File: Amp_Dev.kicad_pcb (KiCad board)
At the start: 2 copper layers, 100 x 100 mm, 760 parts, among them J1 SMA, J10 SMA, J11 CONN_01X02, J12 TEST_1P, J13 SMA, J14 CONN_01X02, J16 TEST_1P, J17 TEST_1P, J18 TEST_1P, J2 SMA, J20 SMA, J21 SMA, J22 SMA, J3 TEST_1P, J4 TEST_1P, J5 CONN_01X03, J6 TEST_1P, J7 CONN_01X03, J8 TEST_1P, J9 TEST_1P, Q1 DMN2075U, U1 MML09211H, U2 RF6886, U3 LMV358, U4 SN74LVC1G17, U5 TLV702, U6 LTC2644, U7 RT9183

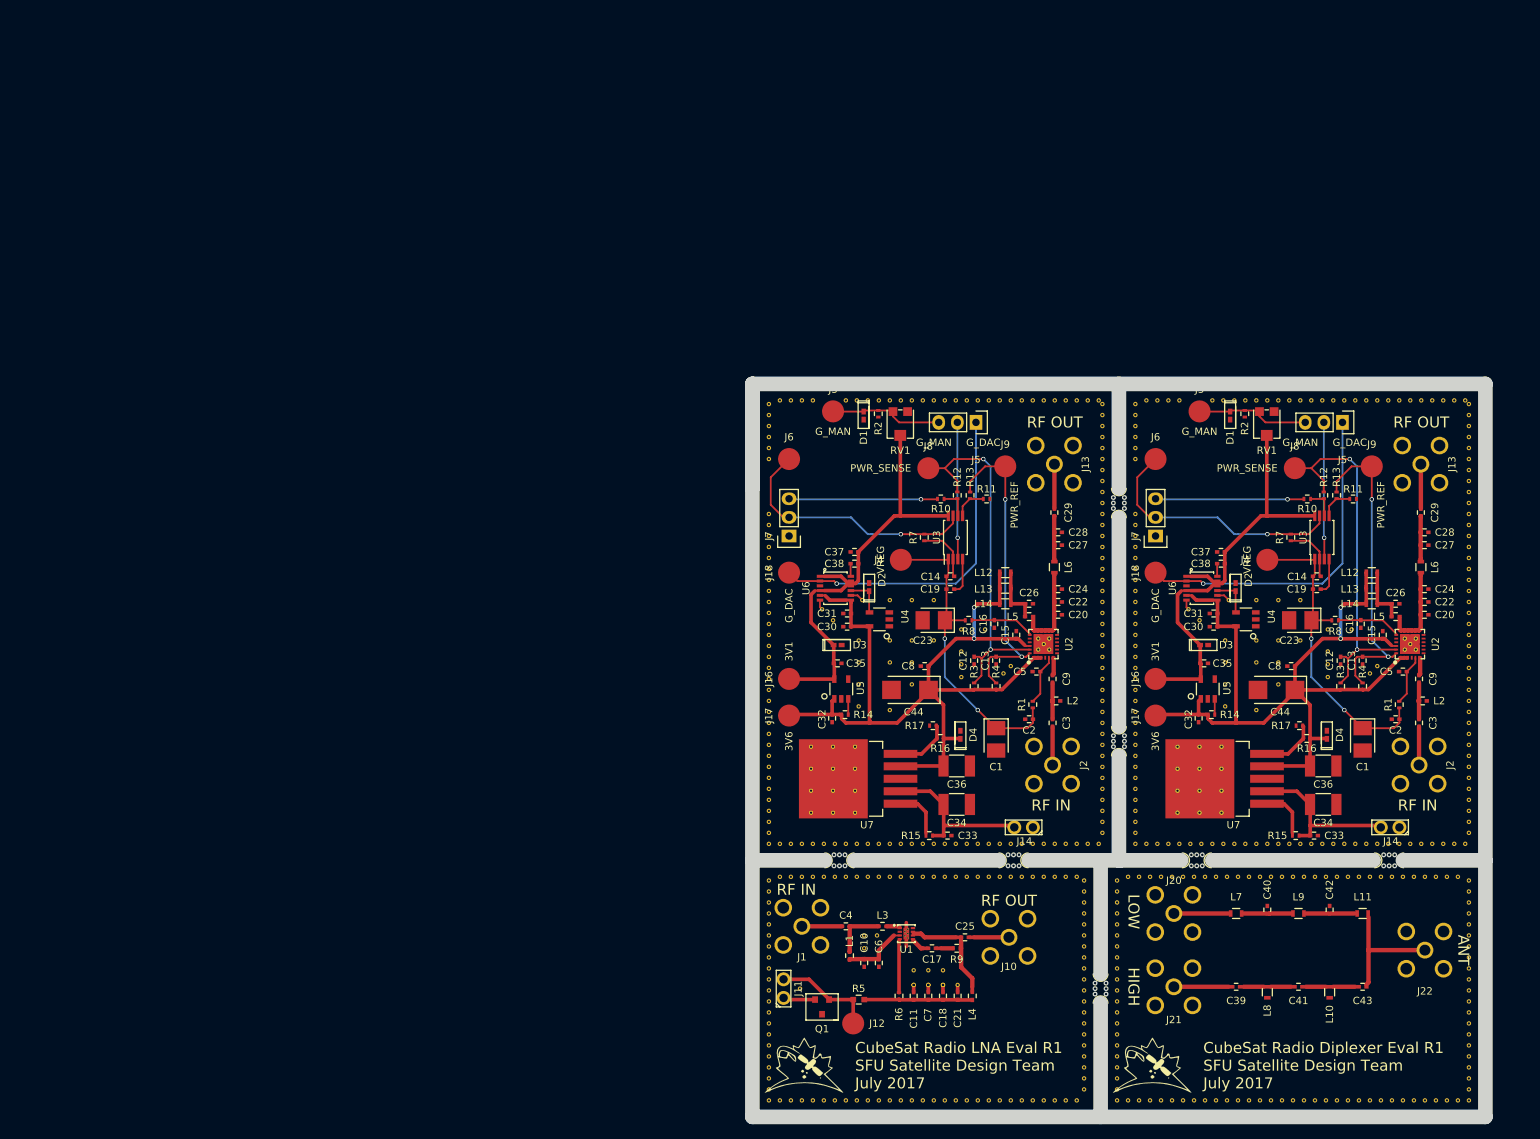
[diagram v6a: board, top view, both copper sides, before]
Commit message: added PA control header. resolves #7
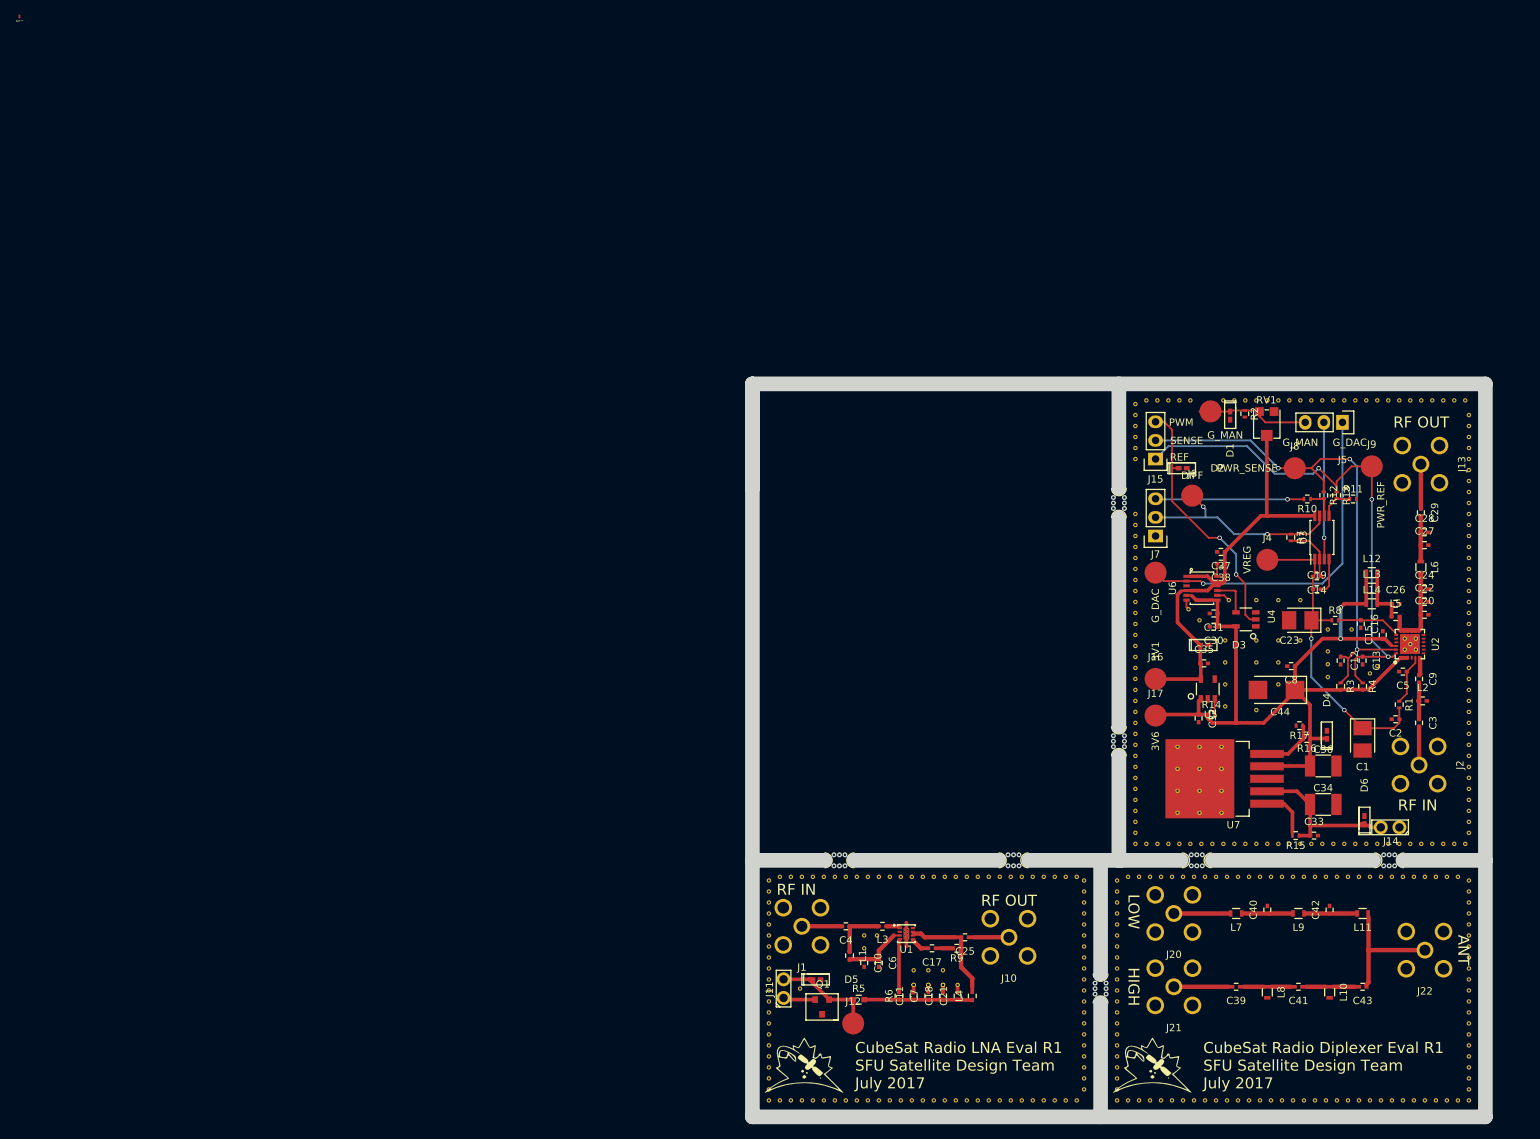
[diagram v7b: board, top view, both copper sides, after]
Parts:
- removed the C1 at (133.2, 98.5)
- removed the C12 at (130.2, 87.8)
- removed the C13 at (133.2, 87.8)
- removed the C14 at (127.0, 76.2)
- removed the C15 at (136.0, 84.2)
- removed the C16 at (133.0, 82.8)
- removed the C19 at (127.0, 78.0)
- removed the C2 at (137.8, 95.8)
- removed the C20 at (141.7, 81.5)
- removed the C22 at (141.7, 79.8)
- removed the C23 at (124.8, 82.2)
- removed the C24 at (141.7, 78.0)
- removed the C26 at (137.8, 80.0)
- removed the C27 at (141.7, 72.0)
- removed the C28 at (141.7, 70.2)
- removed the C29 at (141.2, 67.5)
- removed the C3 at (140.9, 96.2)
- removed the C30 at (112.9, 83.1)
- removed the C31 at (112.9, 81.3)
- removed the C32 at (110.9, 95.6)
- removed the C33 at (126.6, 111.6)
- removed the C34 at (127.9, 107.4)
- removed the C35 at (111.6, 88.1)
- removed the C36 at (127.9, 102.1)
- removed the C37 at (113.9, 72.9)
- removed the C38 at (113.9, 74.5)
- removed the C44 at (121.5, 91.8)
- removed the C5 at (138.8, 89.2)
- removed the C8 at (123.5, 88.5)
- removed the C9 at (140.9, 90.2)
- removed the D1 at (115.2, 54.3)
- removed the D2 at (115.9, 77.7)
- removed the D3 at (111.6, 85.6)
- removed the D4 at (128.4, 97.9)
- removed the G*** at (107.8, 105.8)
- removed the J13 at (141.2, 61.0)
- removed the J14 at (137.0, 110.5)
- removed the J16 at (105.0, 90.2)
- removed the J17 at (105.0, 95.2)
- removed the J18 at (105.0, 75.8)
- removed the J2 at (140.9, 102.0)
- removed the J3 at (111.0, 53.8)
- removed the J4 at (120.2, 74.0)
- removed the J5 at (130.5, 55.2)
- removed the J6 at (105.0, 60.2)
- removed the J7 at (105.0, 70.8)
- removed the J8 at (124.0, 61.5)
- removed the J9 at (134.5, 61.2)
- removed the L12 at (134.5, 75.8)
- removed the L13 at (134.5, 77.9)
- removed the L14 at (134.5, 80.0)
- removed the L2 at (141.4, 93.2)
- removed the L5 at (137.8, 81.8)
- removed the L6 at (141.2, 75.0)
- removed the R1 at (138.2, 93.8)
- removed the R10 at (125.7, 65.7)
- removed the R11 at (131.9, 65.7)
- removed the R12 at (128.0, 65.2)
- removed the R13 at (129.7, 65.2)
- removed the R14 at (112.6, 95.1)
- removed the R15 at (124.1, 111.6)
- removed the R16 at (125.6, 98.4)
- removed the R17 at (124.6, 96.6)
- removed the R2 at (117.2, 54.1)
- removed the R3 at (130.2, 91.2)
- removed the R4 at (133.2, 91.2)
- removed the R7 at (123.5, 71.0)
- removed the R8 at (129.5, 82.2)
- removed the REF** at (139.0, 84.8)
- removed the REF** at (102.2, 109.8)
- removed the REF** at (147.8, 73.8)
- removed the REF** at (147.8, 72.2)
- removed the REF** at (147.8, 70.8)
- removed the REF** at (147.8, 69.2)
- removed the REF** at (147.8, 67.8)
- removed the REF** at (147.8, 66.2)
- removed the REF** at (147.8, 64.8)
- removed the REF** at (147.8, 63.2)
- removed the REF** at (147.8, 61.8)
- removed the REF** at (147.8, 60.2)
- removed the REF** at (102.2, 108.2)
- removed the REF** at (147.8, 58.8)
- removed the REF** at (147.8, 57.2)
- removed the REF** at (147.8, 55.8)
- removed the REF** at (147.8, 54.2)
- removed the REF** at (147.8, 52.8)
- removed the REF** at (103.8, 52.2)
- removed the REF** at (105.2, 52.2)
- removed the REF** at (106.8, 52.2)
- removed the REF** at (108.2, 52.2)
- removed the REF** at (112.8, 52.2)
- removed the REF** at (102.2, 106.8)
- removed the REF** at (114.2, 52.2)
- removed the REF** at (115.8, 52.2)
- removed the REF** at (117.2, 52.2)
- removed the REF** at (118.8, 52.2)
- removed the REF** at (120.2, 52.2)
- removed the REF** at (121.8, 52.2)
- removed the REF** at (123.2, 52.2)
- removed the REF** at (124.8, 52.2)
- removed the REF** at (126.2, 52.2)
- removed the REF** at (127.8, 52.2)
- removed the REF** at (102.2, 105.2)
- removed the REF** at (129.2, 52.2)
- removed the REF** at (130.8, 52.2)
- removed the REF** at (132.2, 52.2)
- removed the REF** at (133.8, 52.2)
- removed the REF** at (135.2, 52.2)
- removed the REF** at (136.8, 52.2)
- removed the REF** at (138.2, 52.2)
- removed the REF** at (139.8, 52.2)
- removed the REF** at (141.2, 52.2)
- removed the REF** at (142.8, 52.2)
- removed the REF** at (102.2, 103.8)
- removed the REF** at (144.2, 52.2)
- removed the REF** at (145.8, 52.2)
- removed the REF** at (147.2, 52.2)
- removed the REF** at (128.5, 90.0)
- removed the REF** at (128.5, 88.2)
- removed the REF** at (128.5, 86.5)
- removed the REF** at (134.2, 89.5)
- removed the REF** at (128.5, 83.5)
- removed the REF** at (131.8, 83.5)
- removed the REF** at (108.0, 99.5)
- removed the REF** at (102.2, 102.2)
- removed the REF** at (111.0, 99.5)
- removed the REF** at (114.0, 99.5)
- removed the REF** at (108.0, 102.5)
- removed the REF** at (111.0, 102.5)
- removed the REF** at (114.0, 102.5)
- removed the REF** at (108.0, 105.5)
- removed the REF** at (111.0, 105.5)
- removed the REF** at (114.0, 105.5)
- removed the REF** at (108.0, 108.5)
- removed the REF** at (111.0, 108.5)
- removed the REF** at (102.2, 100.8)
- removed the REF** at (114.0, 108.5)
- removed the REF** at (109.5, 80.8)
- removed the REF** at (118.8, 79.5)
- removed the REF** at (121.8, 79.5)
- removed the REF** at (124.8, 79.5)
- removed the REF** at (118.8, 85.0)
- removed the REF** at (124.8, 85.0)
- removed the REF** at (121.8, 85.0)
- removed the REF** at (118.8, 88.0)
- removed the REF** at (121.8, 88.0)
- removed the REF** at (102.2, 99.2)
- removed the REF** at (118.8, 94.5)
- removed the REF** at (121.8, 91.0)
- removed the REF** at (111.0, 82.2)
- removed the REF** at (114.5, 85.0)
- removed the REF** at (114.5, 88.0)
- removed the REF** at (114.5, 91.0)
- removed the REF** at (114.5, 94.0)
- removed the REF** at (102.2, 97.8)
- removed the REF** at (102.2, 96.2)
- removed the REF** at (139.0, 86.2)
- removed the REF** at (102.2, 94.8)
- removed the REF** at (102.2, 93.2)
- removed the REF** at (102.2, 91.8)
- removed the REF** at (102.2, 90.2)
- removed the REF** at (102.2, 88.8)
- removed the REF** at (102.2, 87.2)
- removed the REF** at (102.2, 85.8)
- removed the REF** at (102.2, 84.2)
- removed the REF** at (102.2, 82.8)
- removed the REF** at (102.2, 81.2)
- removed the REF** at (140.5, 86.2)
- removed the REF** at (102.2, 79.8)
- removed the REF** at (102.2, 78.2)
- removed the REF** at (102.2, 76.8)
- removed the REF** at (102.2, 75.2)
- removed the REF** at (102.2, 73.8)
- removed the REF** at (102.2, 72.2)
- removed the REF** at (102.2, 70.8)
- removed the REF** at (102.2, 69.2)
- removed the REF** at (102.2, 67.8)
- removed the REF** at (102.2, 60.2)
- removed the REF** at (140.5, 84.8)
- removed the REF** at (102.2, 58.8)
- removed the REF** at (102.2, 57.2)
- removed the REF** at (102.2, 55.8)
- removed the REF** at (102.2, 54.2)
- removed the REF** at (102.2, 52.8)
- removed the REF** at (197.8, 52.8)
- removed the REF** at (103.8, 112.8)
- removed the REF** at (105.2, 112.8)
- removed the REF** at (106.8, 112.8)
- removed the REF** at (108.2, 112.8)
- removed the REF** at (109.8, 112.8)
- removed the REF** at (139.8, 85.5)
- removed the REF** at (111.2, 112.8)
- removed the REF** at (112.8, 112.8)
- removed the REF** at (114.2, 112.8)
- removed the REF** at (115.8, 112.8)
- removed the REF** at (117.2, 112.8)
- removed the REF** at (118.8, 112.8)
- removed the REF** at (120.2, 112.8)
- removed the REF** at (121.8, 112.8)
- removed the REF** at (123.2, 112.8)
- removed the REF** at (124.8, 112.8)
- removed the REF** at (135.2, 88.5)
- removed the REF** at (126.2, 112.8)
- removed the REF** at (127.8, 112.8)
- removed the REF** at (129.2, 112.8)
- removed the REF** at (130.8, 112.8)
- removed the REF** at (132.2, 112.8)
- removed the REF** at (133.8, 112.8)
- removed the REF** at (135.2, 112.8)
- removed the REF** at (136.8, 112.8)
- removed the REF** at (138.2, 112.8)
- removed the REF** at (139.8, 112.8)
- removed the REF** at (115.0, 79.5)
- removed the REF** at (141.2, 112.8)
- removed the REF** at (142.8, 112.8)
- removed the REF** at (144.2, 112.8)
- removed the REF** at (145.8, 112.8)
- removed the REF** at (147.2, 112.8)
- removed the REF** at (147.8, 111.2)
- removed the REF** at (147.8, 109.8)
- removed the REF** at (147.8, 108.2)
- removed the REF** at (147.8, 106.8)
- removed the REF** at (147.8, 105.2)
- removed the REF** at (102.2, 112.8)
- removed the REF** at (147.8, 103.8)
- removed the REF** at (147.8, 102.2)
- removed the REF** at (147.8, 100.8)
- removed the REF** at (147.8, 99.2)
- removed the REF** at (147.8, 97.8)
- removed the REF** at (147.8, 96.2)
- removed the REF** at (147.8, 94.8)
- removed the REF** at (147.8, 93.2)
- removed the REF** at (147.8, 91.8)
- removed the REF** at (147.8, 90.2)
- removed the REF** at (102.2, 111.2)
- removed the REF** at (147.8, 88.8)
- removed the REF** at (147.8, 87.2)
- removed the REF** at (147.8, 85.8)
- removed the REF** at (147.8, 84.2)
- removed the REF** at (147.8, 82.8)
- removed the REF** at (147.8, 81.2)
- removed the REF** at (147.8, 79.8)
- removed the REF** at (147.8, 78.2)
- removed the REF** at (147.8, 76.8)
- removed the REF** at (147.8, 75.2)
- removed the RV1 at (120.2, 55.6)
- removed the U2 at (139.7, 85.5)
- removed the U3 at (127.7, 71.0)
- removed the U4 at (117.3, 82.1)
- removed the U5 at (112.1, 91.6)
- removed the U6 at (111.3, 77.9)
- removed the U7 at (115.6, 103.9)
- added D5: PESD5Zx, SFUSat:PESD57zx, F.Cu at (108.8, 131.2)
- added D6: PESD5Zx, SFUSat:PESD57zx, F.Cu at (183.5, 109.5)
- added J15: CONN_01X03, SFUSat:Socket_Strip_Straight_1x03, F.Cu at (155.0, 60.2)
- added REF**: muwave_stub, muwave_stub, F.Cu at (0.00, 0.00)
- moved D2 17.8 mm to (158.7, 61.5), turned to 0 degrees
- moved J6 7.07 mm to (160.0, 65.2)
- moved REF** 3.00 mm to (159.8, 52.2)
- moved J3 1.50 mm to (162.5, 53.8)
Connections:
- D2 pad 1: Net-(D2-Pad1) -> /MCU_PWM
- U4 pad 4: Net-(D2-Pad1) -> Net-(U4-Pad4)
- U6 pad 9: Net-(D2-Pad1) -> Net-(U4-Pad4)
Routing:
- net /3V6: track 234.1 -> 117.1 mm, vias 4 -> 2
- net /3V1: track 121.3 -> 60.7 mm
- net /G_DAC: track 93.0 -> 46.5 mm, vias 2 -> 1
- net /VREG: track 85.8 -> 42.9 mm, vias 4 -> 2
- net Net-(J6-Pad1): track 70.9 -> 29.5 mm
- net /MCU_PWM: track 0.00 -> 35.6 mm, vias 0 -> 2
- net /PWR_SENSE: track 100.6 -> 70.9 mm, vias 4 -> 3
- net Net-(C33-Pad1): track 44.3 -> 23.7 mm
- net Net-(J7-Pad3): track 40.6 -> 20.3 mm, vias 2 -> 1
- net Net-(J5-Pad2): track 37.4 -> 18.7 mm, vias 2 -> 1
- net /G_MAN: track 31.1 -> 15.5 mm
- net /PWR_REF: track 87.3 -> 72.8 mm, vias 4 -> 3
- net Net-(C20-Pad1): track 24.9 -> 12.5 mm
- net Net-(D2-Pad1): track 10.9 -> 0.00 mm
- net GND: track 27.0 -> 17.1 mm
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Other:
- board text added: "DIFF"
- board text added: "PWM"
- board text added: "REF"
- board text added: "SENSE"

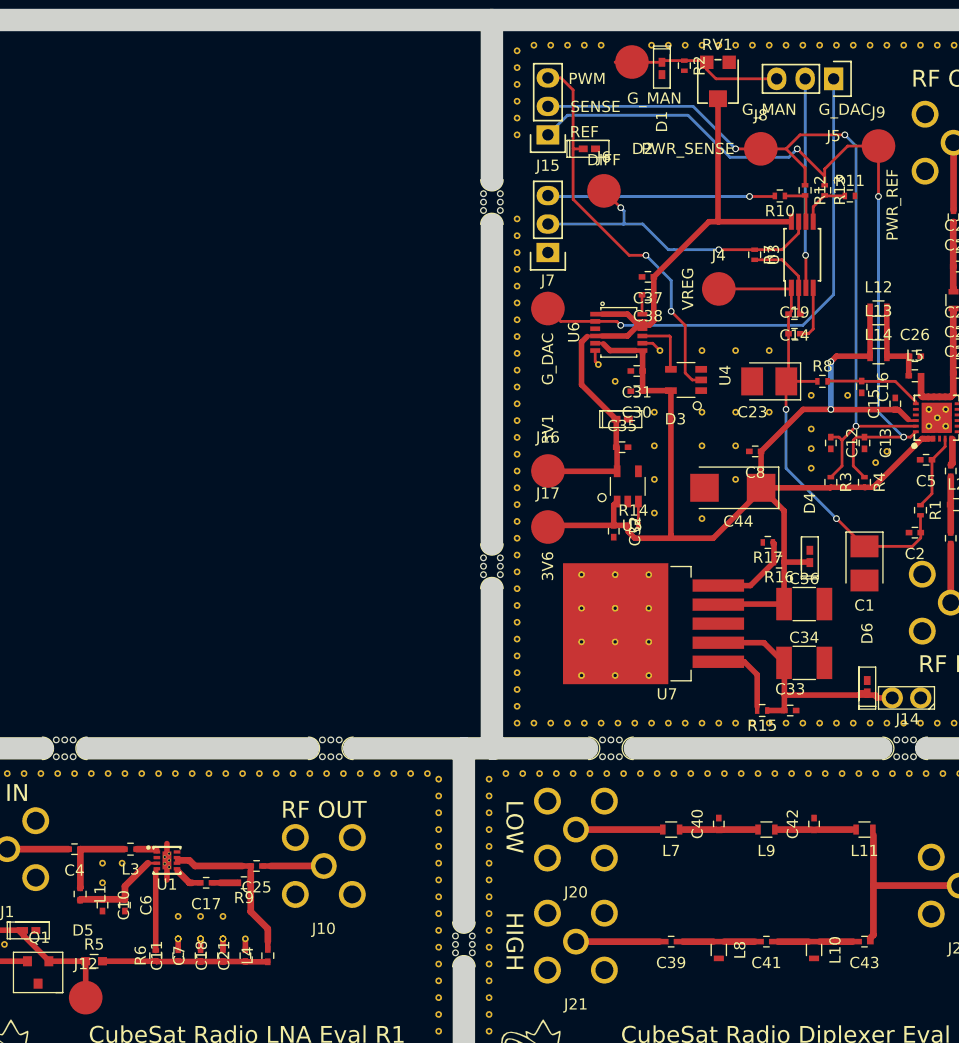
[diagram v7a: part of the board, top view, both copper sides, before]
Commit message: hid test point reference. resolves #10
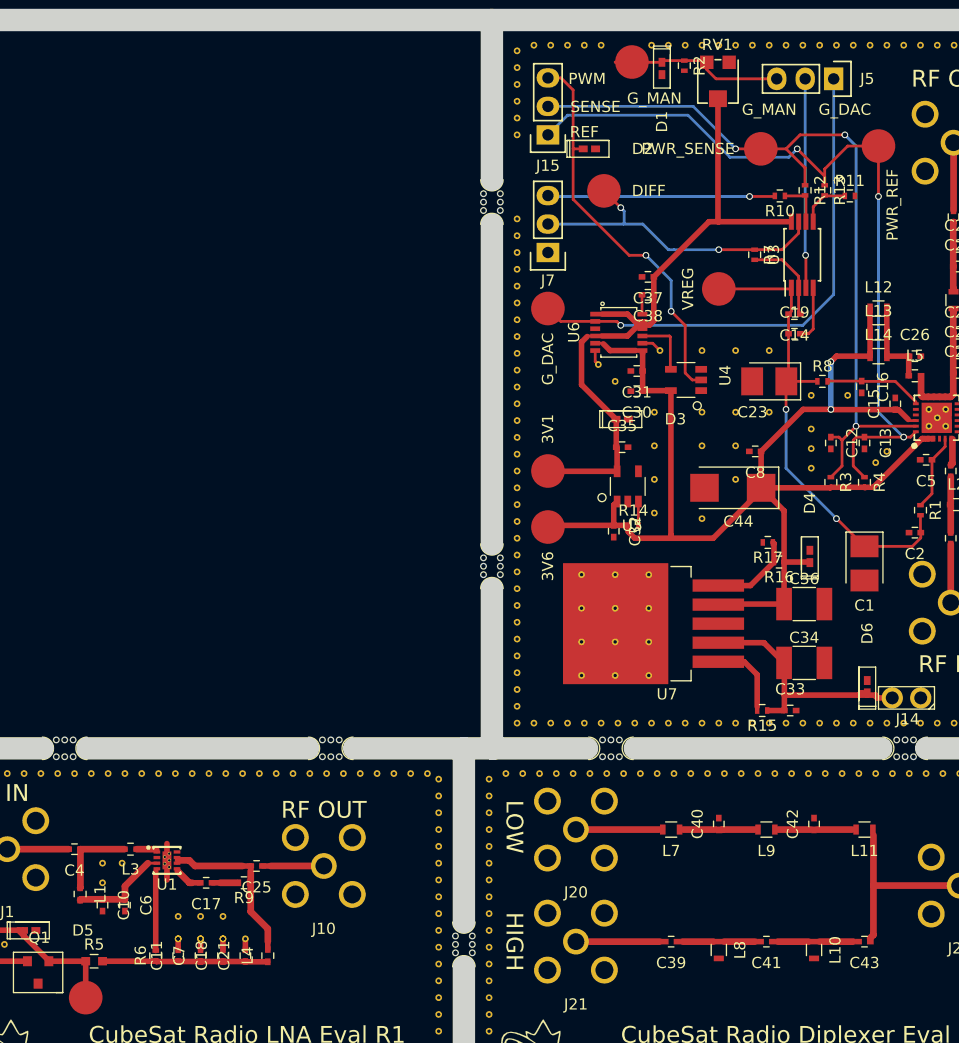
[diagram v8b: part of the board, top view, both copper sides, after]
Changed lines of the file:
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@@
     (tags "Mesurement Point Round SMD Pad 3mm")
     (attr virtual)
-    (fp_text reference J17 (at 0 -3) (layer F.SilkS)
+    (fp_text reference J17 (at 0 -0.5) (layer F.SilkS) hide
       (effects (font (size 1 1) (thickness 0.15)))
     )
@@
     (tags "Mesurement Point Round SMD Pad 3mm")
     (attr virtual)
-    (fp_text reference J16 (at 0 -3) (layer F.SilkS)
+    (fp_text reference J16 (at 0 -0.25) (layer F.SilkS) hide
       (effects (font (size 1 1) (thickness 0.15)))
     )
@@
     (tags "Mesurement Point Round SMD Pad 3mm")
     (attr virtual)
-    (fp_text reference J12 (at 0 -3) (layer F.SilkS)
+    (fp_text reference J12 (at -0.25 -0.75) (layer F.SilkS) hide
       (effects (font (size 1 1) (thickness 0.15)))
     )
@@
     (tags "Mesurement Point Round SMD Pad 3mm")
     (attr virtual)
-    (fp_text reference J9 (at 0 -3) (layer F.SilkS)
+    (fp_text reference J9 (at 0.25 -0.25) (layer F.SilkS) hide
       (effects (font (size 1 1) (thickness 0.15)))
     )
@@
     (tags "Mesurement Point Round SMD Pad 3mm")
     (attr virtual)
-    (fp_text reference J8 (at 0 -3) (layer F.SilkS)
+    (fp_text reference J8 (at 0 -0.75) (layer F.SilkS) hide
       (effects (font (size 1 1) (thickness 0.15)))
     )
@@
     (tags "Mesurement Point Round SMD Pad 3mm")
     (attr virtual)
-    (fp_text reference J6 (at 0 -3) (layer F.SilkS)
+    (fp_text reference J6 (at 0 -0.25) (layer F.SilkS) hide
       (effects (font (size 1 1) (thickness 0.15)))
     )
@@
     (descr "Through hole socket strip")
     (tags "socket strip")
-    (fp_text reference J5 (at 0 -5.1 180) (layer F.SilkS)
+    (fp_text reference J5 (at -3 0 180) (layer F.SilkS)
       (effects (font (size 1 1) (thickness 0.15)))
     )
@@
     (tags "Mesurement Point Round SMD Pad 3mm")
     (attr virtual)
-    (fp_text reference J4 (at 0 -3) (layer F.SilkS)
+    (fp_text reference J4 (at 0 -3) (layer F.SilkS) hide
       (effects (font (size 1 1) (thickness 0.15)))
     )
@@
     (effects (font (size 1 1) (thickness 0.15)))
   )
-  (gr_text DIFF (at 160 62.5) (layer F.SilkS)
+  (gr_text DIFF (at 164 65.25) (layer F.SilkS)
     (effects (font (size 1 1) (thickness 0.15)))
   )
